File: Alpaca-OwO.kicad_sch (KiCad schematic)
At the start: 43 parts, among them J1 SWD, J2 PS360 ST1, J3 PS360 ST2, J4 Stick, J5 USB_B, J6 Pwny Pr0t, J7 I2C Quick connect, Q1 CJL3415, SW1 Reset, SW2 I2C Pullup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

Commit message: Coarse placement
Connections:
- net +1V1: now also C6.2; no longer C6.1
- net GND: now also C6.1; no longer C6.2
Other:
- moved on the sheet: C6
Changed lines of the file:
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@@
     (pin "2")
   )
-  (symbol (lib_id "Device:C_Small") (at 109.855 41.275 180) (unit 1)
+  (symbol (lib_id "Device:C_Small") (at 109.855 41.275 0) (unit 1)
     (in_bom yes) (on_board yes) (fields_autoplaced)
-    (property "Reference" "C6" (id 0) (at 112.1791 40.4339 0)
-      (effects (font (size 1.27 1.27)) (justify right))
+    (property "Reference" "C6" (id 0) (at 113.03 40.0112 0)
+      (effects (font (size 1.27 1.27)) (justify left))
     )
-    (property "Value" "100nF" (id 1) (at 112.1791 42.9708 0)
-      (effects (font (size 1.27 1.27)) (justify right))
+    (property "Value" "100nF" (id 1) (at 113.03 42.5512 0)
+      (effects (font (size 1.27 1.27)) (justify left))
     )
     (property "Footprint" "Capacitor_SMD:C_0603_1608Metric" (id 2) (at 109.855 41.275 0)

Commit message: Routing checkpoint
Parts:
- Y1: footprint Crystal:Crystal_HC49-U_Vertical -> Crystal:Crystal_HC49-4H_Vertical
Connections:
- net +3V3: now also C8.1; no longer C8.2
- net GND: now also C4.1, C8.2; no longer C4.2, C8.1
- net at R2.1, Y1.1: now also C4.2; no longer C4.1
- net UPIN_D-: now reaches R4.1, U2.47 (USB_DP)
- net UPIN_D+: now reaches R3.1, U2.46 (USB_DM)
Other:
- moved on the sheet: C3, C4, C8, Y1

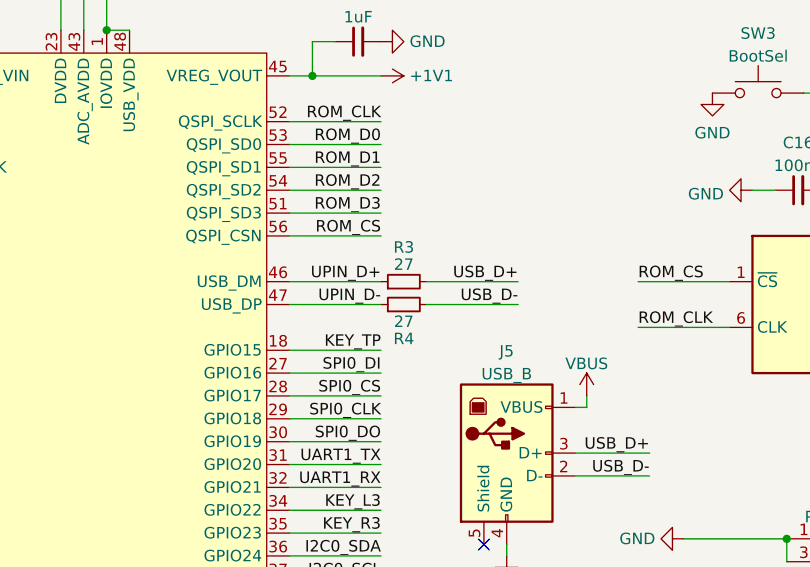
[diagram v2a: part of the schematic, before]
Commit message: Fix various issues.
- USB DM/DP are reversed.
- Minimum via OD for JLC should be 0.45mm (technically 0.4mm is also accepted but with a big cost penalty).
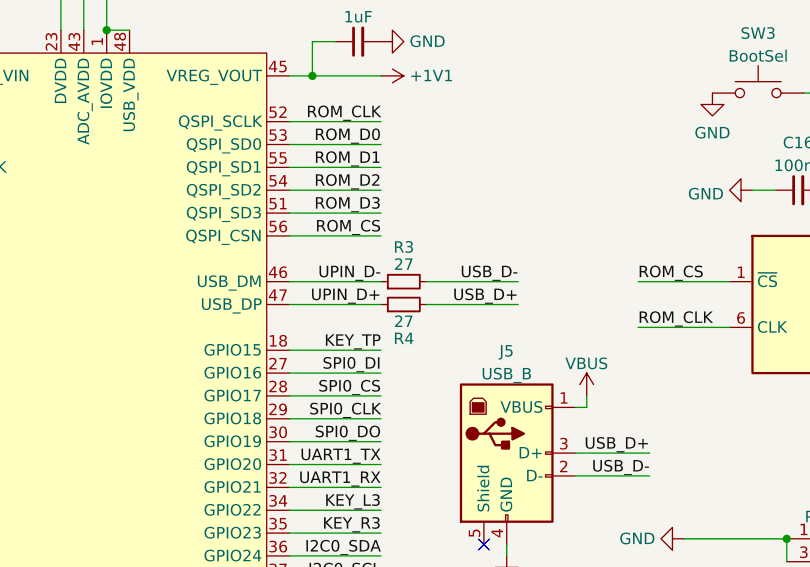
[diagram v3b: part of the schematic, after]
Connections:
- net UPIN_D+: now also R4.1, U2.47 (USB_DP); no longer R3.1, U2.46 (USB_DM)
- net UPIN_D-: now also R3.1, U2.46 (USB_DM); no longer R4.1, U2.47 (USB_DP)
- net USB_D+: now also R4.2; no longer R3.2
- net USB_D-: now also R3.2; no longer R4.2
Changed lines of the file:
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@@
     (effects (font (size 1.27 1.27)) (justify right bottom))
   )
-  (label "UPIN_D-" (at 166.37 80.01 180)
+  (label "UPIN_D-" (at 166.37 77.47 180)
     (effects (font (size 1.27 1.27)) (justify right bottom))
   )
@@
     (effects (font (size 1.27 1.27)) (justify left bottom))
   )
-  (label "UPIN_D+" (at 166.37 77.47 180)
+  (label "UPIN_D+" (at 166.37 80.01 180)
     (effects (font (size 1.27 1.27)) (justify right bottom))
   )
@@
     (effects (font (size 1.27 1.27)) (justify left bottom))
   )
-  (label "USB_D+" (at 181.61 77.47 180)
+  (label "USB_D+" (at 181.61 80.01 180)
     (effects (font (size 1.27 1.27)) (justify right bottom))
   )
@@
     (effects (font (size 1.27 1.27)) (justify left bottom))
   )
-  (label "USB_D-" (at 181.61 80.01 180)
+  (label "USB_D-" (at 181.61 77.47 180)
     (effects (font (size 1.27 1.27)) (justify right bottom))
   )

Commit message: Add metadata.
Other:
- company: (none) -> dogtopus
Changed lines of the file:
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@@
     (date "2022-02-27")
     (rev "v1.0")
+    (company "dogtopus")
   )
   (junction (at 86.36 42.545) (diameter 0) (color 0 0 0 0)

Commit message: V1.01 rework.
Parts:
- SW1, SW3: footprint Button_Switch_THT:SW_Tactile_Straight_KSA0Axx1LFTR -> Button_Switch_THT:SW_PUSH_6mm
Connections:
- net GND: now also SW1.2, SW3.2; no longer SW1.1, SW3.1
- net ~{RESET}: now also SW1.1; no longer SW1.2
- net at R7.1: now also SW3.1; no longer SW3.2
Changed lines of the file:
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@@
     (title "Alpaca-OwO")
     (date "2022-02-27")
-    (rev "v1.0")
+    (rev "v1.01")
     (company "dogtopus")
   )
@@
     (pin "2")
   )
-  (symbol (lib_id "Switch:SW_Push") (at 46.355 68.58 0) (unit 1)
-    (in_bom yes) (on_board yes) (fields_autoplaced)
-    (property "Reference" "SW1" (id 0) (at 46.355 61.9592 0))
-    (property "Value" "Reset" (id 1) (at 46.355 64.4961 0))
-    (property "Footprint" "Button_Switch_THT:SW_Tactile_Straight_KSA0Axx1LFTR" (id 2) (at 46.355 63.5 0)
+  (symbol (lib_id "Switch:SW_Push") (at 46.355 68.58 0) (mirror y) (unit 1)
+    (in_bom yes) (on_board yes) (fields_autoplaced)
+    (property "Reference" "SW1" (id 0) (at 46.355 60.96 0))
+    (property "Value" "Reset" (id 1) (at 46.355 63.5 0))
+    (property "Footprint" "Button_Switch_THT:SW_PUSH_6mm" (id 2) (at 46.355 63.5 0)
       (effects (font (size 1.27 1.27)) hide)
     )
@@
     (pin "2")
   )
-  (symbol (lib_id "Switch:SW_Push") (at 208.28 56.515 0) (unit 1)
-    (in_bom yes) (on_board yes) (fields_autoplaced)
-    (property "Reference" "SW3" (id 0) (at 208.28 49.8942 0))
-    (property "Value" "BootSel" (id 1) (at 208.28 52.4311 0))
-    (property "Footprint" "Button_Switch_THT:SW_Tactile_Straight_KSA0Axx1LFTR" (id 2) (at 208.28 51.435 0)
+  (symbol (lib_id "Switch:SW_Push") (at 208.28 56.515 0) (mirror y) (unit 1)
+    (in_bom yes) (on_board yes) (fields_autoplaced)
+    (property "Reference" "SW3" (id 0) (at 208.28 48.26 0))
+    (property "Value" "BootSel" (id 1) (at 208.28 50.8 0))
+    (property "Footprint" "Button_Switch_THT:SW_PUSH_6mm" (id 2) (at 208.28 51.435 0)
       (effects (font (size 1.27 1.27)) hide)
     )
@@
     )
     (path "/3c126155-92ea-4212-9983-c5116bfe45bf"
-      (reference "SW1") (unit 1) (value "Reset") (footprint "Button_Switch_THT:SW_Tactile_Straight_KSA0Axx1LFTR")
+      (reference "SW1") (unit 1) (value "Reset") (footprint "Button_Switch_THT:SW_PUSH_6mm")
     )
     (path "/8acb05ec-8539-4ff7-8e45-31727d5278d9"
@@
     )
     (path "/53c22354-630c-466e-b843-a7e0e45672e7"
-      (reference "SW3") (unit 1) (value "BootSel") (footprint "Button_Switch_THT:SW_Tactile_Straight_KSA0Axx1LFTR")
+      (reference "SW3") (unit 1) (value "BootSel") (footprint "Button_Switch_THT:SW_PUSH_6mm")
     )
     (path "/d3893f63-dd1c-4e09-b64e-0a9180cbb629"

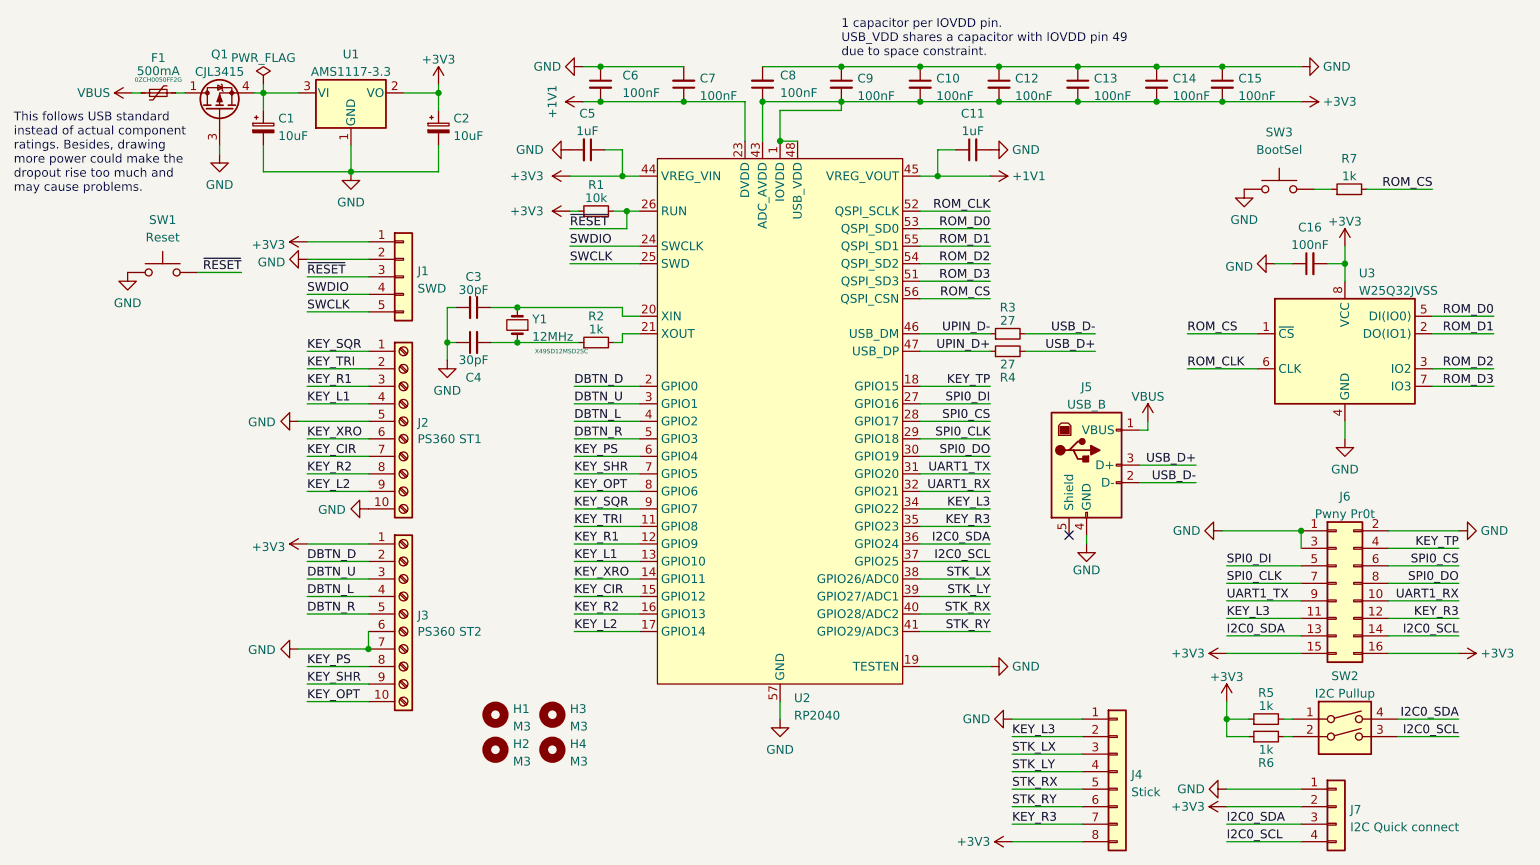
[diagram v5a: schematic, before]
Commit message: Add some PCBA info.
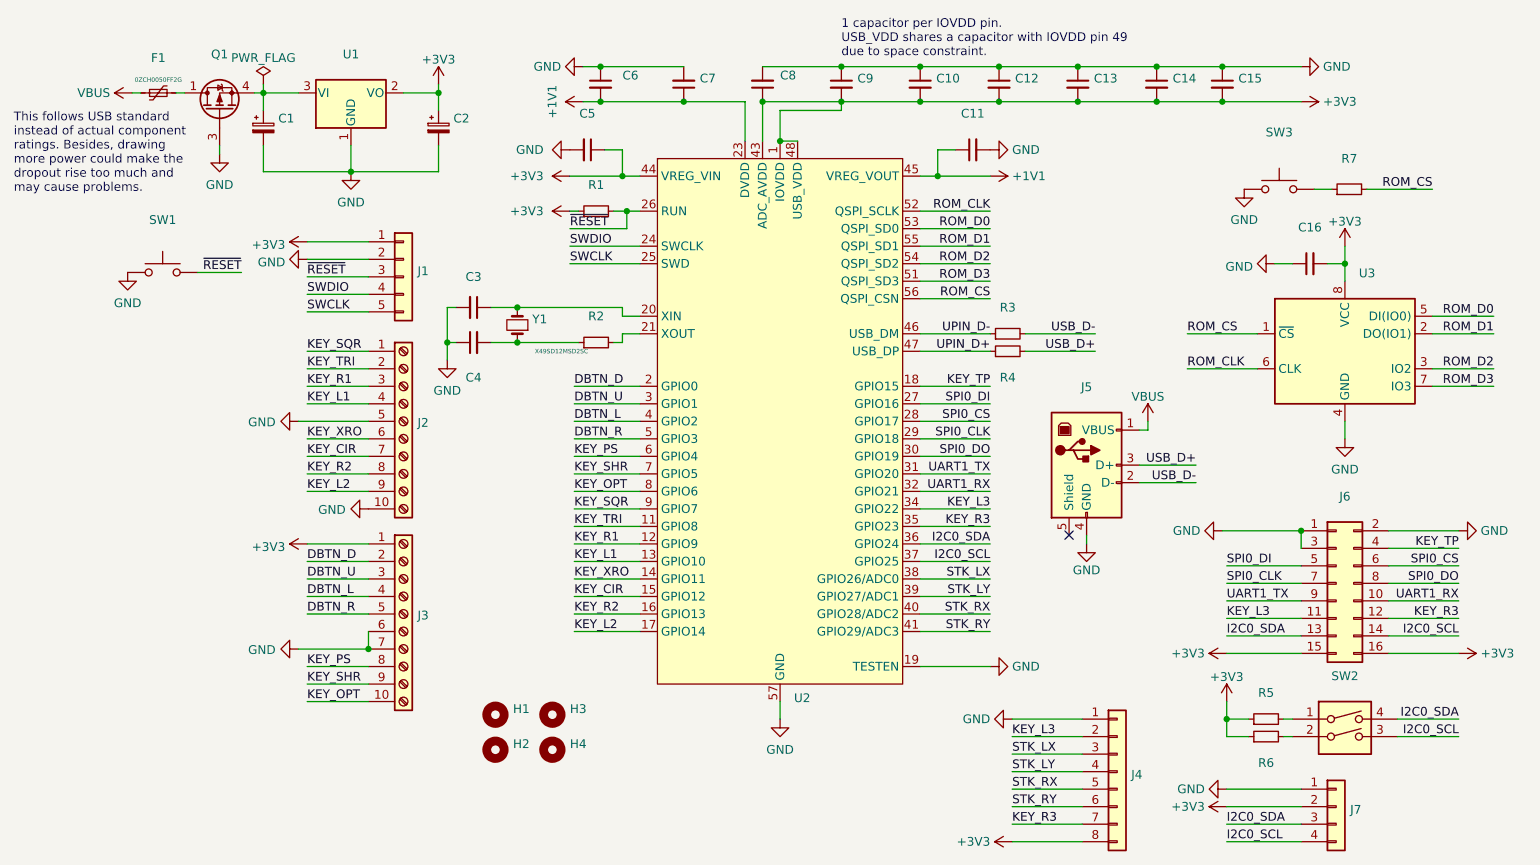
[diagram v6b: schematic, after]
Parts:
- C1, C2: value 10uF -> (none); footprint Capacitor_Tantalum_SMD:CP_EIA-3216-18_Kemet-A -> (none); JLC (none) -> CASE-A_3216; LCSC (none) -> C7171
- C10, C12, C13, C14, C15, C16, C6, C7, C8, C9: value 100nF -> (none); footprint Capacitor_SMD:C_0603_1608Metric -> (none)
- C11, C5: value 1uF -> (none); footprint Capacitor_SMD:C_0603_1608Metric -> (none)
- C3, C4: value 30pF -> (none); footprint Capacitor_SMD:C_0603_1608Metric -> (none)
- F1: value 500mA -> (none); footprint Fuse:Fuse_1210_3225Metric -> (none); Comments (none) -> Used JDT ASMD1210-050 for JLCPCBA as a replacement part.; JLC (none) -> 1210; LCSC (none) -> C135348
- H1, H2, H3, H4: value M3 -> (none); footprint MountingHole:MountingHole_3.2mm_M3_ISO7380 -> (none)
- J1: value SWD -> (none); footprint Connector_PinHeader_2.54mm:PinHeader_1x05_P2.54mm_Vertical -> (none)
- J2: value PS360 ST1 -> (none); footprint Connector_Phoenix_MC:PhoenixContact_MC_1,5_10-G-3.5_1x10_P3.50mm_Horizontal -> (none)
- J3: value PS360 ST2 -> (none); footprint Connector_Phoenix_MC:PhoenixContact_MC_1,5_10-G-3.5_1x10_P3.50mm_Horizontal -> (none)
- J4: value Stick -> (none); footprint Connector_PinHeader_2.54mm:PinHeader_1x08_P2.54mm_Vertical -> (none)
- J5: value USB_B -> (none); footprint Connector_USB:USB_B_OST_USB-B1HSxx_Horizontal -> (none)
- J6: value Pwny Pr0t -> (none); footprint Connector_PinHeader_2.54mm:PinHeader_2x08_P2.54mm_Vertical -> (none)
- J7: value I2C Quick connect -> (none); footprint Connector_JST:JST_SH_SM04B-SRSS-TB_1x04-1MP_P1.00mm_Horizontal -> (none)
- Q1: value CJL3415 -> (none); footprint Package_TO_SOT_SMD:SOT-23-6 -> (none); JLC (none) -> SOT-23-6; LCSC (none) -> C114069
- R1: value 10k -> (none); footprint Resistor_SMD:R_0603_1608Metric -> (none)
- R2, R5, R6, R7: value 1k -> (none); footprint Resistor_SMD:R_0603_1608Metric -> (none)
- R3, R4: value 27 -> (none); footprint Resistor_SMD:R_0603_1608Metric -> (none)
- SW1: value Reset -> (none); footprint Button_Switch_THT:SW_PUSH_6mm -> (none)
- SW2: value I2C Pullup -> (none); footprint Button_Switch_THT:SW_DIP_SPSTx02_Slide_9.78x7.26mm_W7.62mm_P2.54mm -> (none)
- SW3: value BootSel -> (none); footprint Button_Switch_THT:SW_PUSH_6mm -> (none)
- U1: value AMS1117-3.3 -> (none); footprint Package_TO_SOT_SMD:SOT-223-3_TabPin2 -> (none)
- U2: value RP2040 -> (none); footprint private:QFN-56-1EP_7x7mm_P0.4mm_EP3.2x3.2mm_ThermalVias -> (none)
- U3: value W25Q32JVSS -> (none); footprint Package_SO:SOIC-8_5.23x5.23mm_P1.27mm -> (none)
- Y1: value 12MHz -> (none); footprint Crystal:Crystal_HC49-4H_Vertical -> (none); JLC (none) -> HC-49S; LCSC (none) -> C16369

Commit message: Flip I2C traces up and some general cleanups
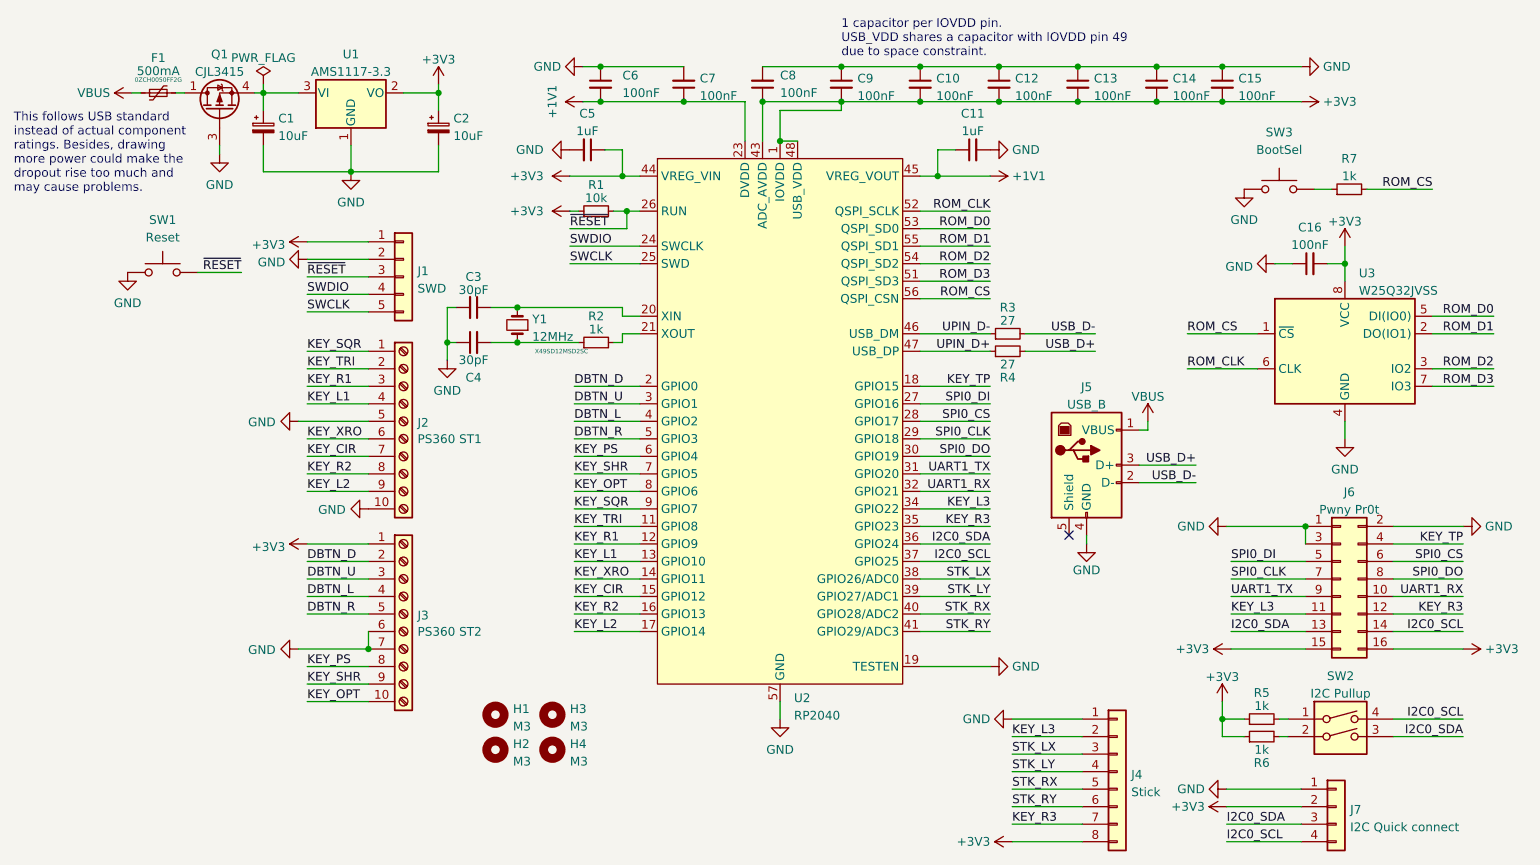
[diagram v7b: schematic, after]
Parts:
- C1, C2: value (none) -> 10uF; footprint (none) -> Capacitor_Tantalum_SMD:CP_EIA-3216-18_Kemet-A
- C10, C12, C13, C14, C15, C16, C6, C7, C8, C9: value (none) -> 100nF; footprint (none) -> Capacitor_SMD:C_0603_1608Metric
- C11, C5: value (none) -> 1uF; footprint (none) -> Capacitor_SMD:C_0603_1608Metric
- C3, C4: value (none) -> 30pF; footprint (none) -> Capacitor_SMD:C_0603_1608Metric
- F1: value (none) -> 500mA; footprint (none) -> Fuse:Fuse_1210_3225Metric
- H1, H2, H3, H4: value (none) -> M3; footprint (none) -> MountingHole:MountingHole_3.2mm_M3_ISO7380
- J1: value (none) -> SWD; footprint (none) -> Connector_PinHeader_2.54mm:PinHeader_1x05_P2.54mm_Vertical
- J2: value (none) -> PS360 ST1; footprint (none) -> Connector_Phoenix_MC:PhoenixContact_MC_1,5_10-G-3.5_1x10_P3.50mm_Horizontal
- J3: value (none) -> PS360 ST2; footprint (none) -> Connector_Phoenix_MC:PhoenixContact_MC_1,5_10-G-3.5_1x10_P3.50mm_Horizontal
- J4: value (none) -> Stick; footprint (none) -> Connector_PinHeader_2.54mm:PinHeader_1x08_P2.54mm_Vertical
- J5: value (none) -> USB_B; footprint (none) -> Connector_USB:USB_B_OST_USB-B1HSxx_Horizontal
- J6: value (none) -> Pwny Pr0t; footprint (none) -> Connector_PinHeader_2.54mm:PinHeader_2x08_P2.54mm_Vertical
- J7: value (none) -> I2C Quick connect; footprint (none) -> Connector_JST:JST_SH_SM04B-SRSS-TB_1x04-1MP_P1.00mm_Horizontal
- Q1: value (none) -> CJL3415; footprint (none) -> Package_TO_SOT_SMD:SOT-23-6
- R1: value (none) -> 10k; footprint (none) -> Resistor_SMD:R_0603_1608Metric
- R2, R5, R6, R7: value (none) -> 1k; footprint (none) -> Resistor_SMD:R_0603_1608Metric
- R3, R4: value (none) -> 27; footprint (none) -> Resistor_SMD:R_0603_1608Metric
- SW1: value (none) -> Reset; footprint (none) -> Button_Switch_THT:SW_PUSH_6mm
- SW2: value (none) -> I2C Pullup; footprint (none) -> Button_Switch_THT:SW_DIP_SPSTx02_Slide_9.78x7.26mm_W7.62mm_P2.54mm
- SW3: value (none) -> BootSel; footprint (none) -> Button_Switch_THT:SW_PUSH_6mm
- U1: value (none) -> AMS1117-3.3; footprint (none) -> Package_TO_SOT_SMD:SOT-223-3_TabPin2
- U2: value (none) -> RP2040; footprint (none) -> private:QFN-56-1EP_7x7mm_P0.4mm_EP3.2x3.2mm_ThermalVias
- U3: value (none) -> W25Q32JVSS; footprint (none) -> Package_SO:SOIC-8_5.23x5.23mm_P1.27mm
- Y1: value (none) -> 12MHz; footprint (none) -> Crystal:Crystal_HC49-4H_Vertical
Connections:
- net I2C0_SCL: now also SW2.4; no longer SW2.3
- net I2C0_SDA: now also SW2.3; no longer SW2.4
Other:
- moved on the sheet: J6, R5, R6, SW2
